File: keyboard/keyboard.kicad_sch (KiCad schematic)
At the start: 29 parts, among them SW10 KH-6X6X6H-STM, SW11 KH-6X6X6H-STM, SW12 KH-6X6X6H-STM, SW13 KH-6X6X6H-STM, SW14 KH-6X6X6H-STM, SW3 KH-6X6X6H-STM, SW4 KH-6X6X6H-STM, SW5 KH-6X6X6H-STM, SW6 KH-6X6X6H-STM, SW7 KH-6X6X6H-STM, SW8 KH-6X6X6H-STM, SW9 KH-6X6X6H-STM, U12 TM1638

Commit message: feat: 新增点阵屏键盘小板
新增点阵屏小板的工程，并删除主项目的 sch
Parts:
- removed C19: 100pF, Capacitor_SMD:C_0603_1608Metric, symbol Device:C
- removed R11: 10k, PCM_SparkFun-Resistor:R_0603_1608Metric, symbol PCM_SparkFun-Resistor:R
- added FPC1: HC-FPC-05-10-5RLTAG, lcsc_footprints:C5213728_FPC-SMD_5P-P0_50_HCTL_HC-FPC-05-10-5RLTAG, symbol lcsc_imported:HC-FPC-05-10-5RLTAG
- D3, D4, D5, D6, D7, D8: footprint PCM_Diode_SMD_AKL:D_SOD-123 -> Diode_SMD:D_SOD-123
- R12, R13: footprint PCM_SparkFun-Resistor:R_0603_1608Metric -> Resistor_SMD:R_0603_1608Metric
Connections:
- net 5V_IN: now also FPC1.1
- net GND_IN: now also FPC1.2
- net CLK: no longer names the net of C20.1, R12.1, U12.27 (CLK)
- net CLK: now also FPC1.4
- net DIO: no longer names the net of C21.1, R13.1, U12.26 (DIO)
- net DIO: now also FPC1.5
- net STB: no longer names the net of U12.28 (STB)
- net STB: now also FPC1.3
- no-connect marks 19 -> 21
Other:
- moved on the sheet: C22, C23

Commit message: update: 添加按键小板电源指示灯并优化布线
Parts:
- added D1: LED, LED_SMD:LED_0603_1608Metric, symbol Device:LED
- added R14: 4.7k, Resistor_SMD:R_0603_1608Metric, symbol PCM_SparkFun-Resistor:R
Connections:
- net 5V_IN renamed +5V
- net +5V: now also D1.2 (A)
- net GND_IN renamed GND
- net GND: now also R14.1
- new net: D1.1 (K), R14.2

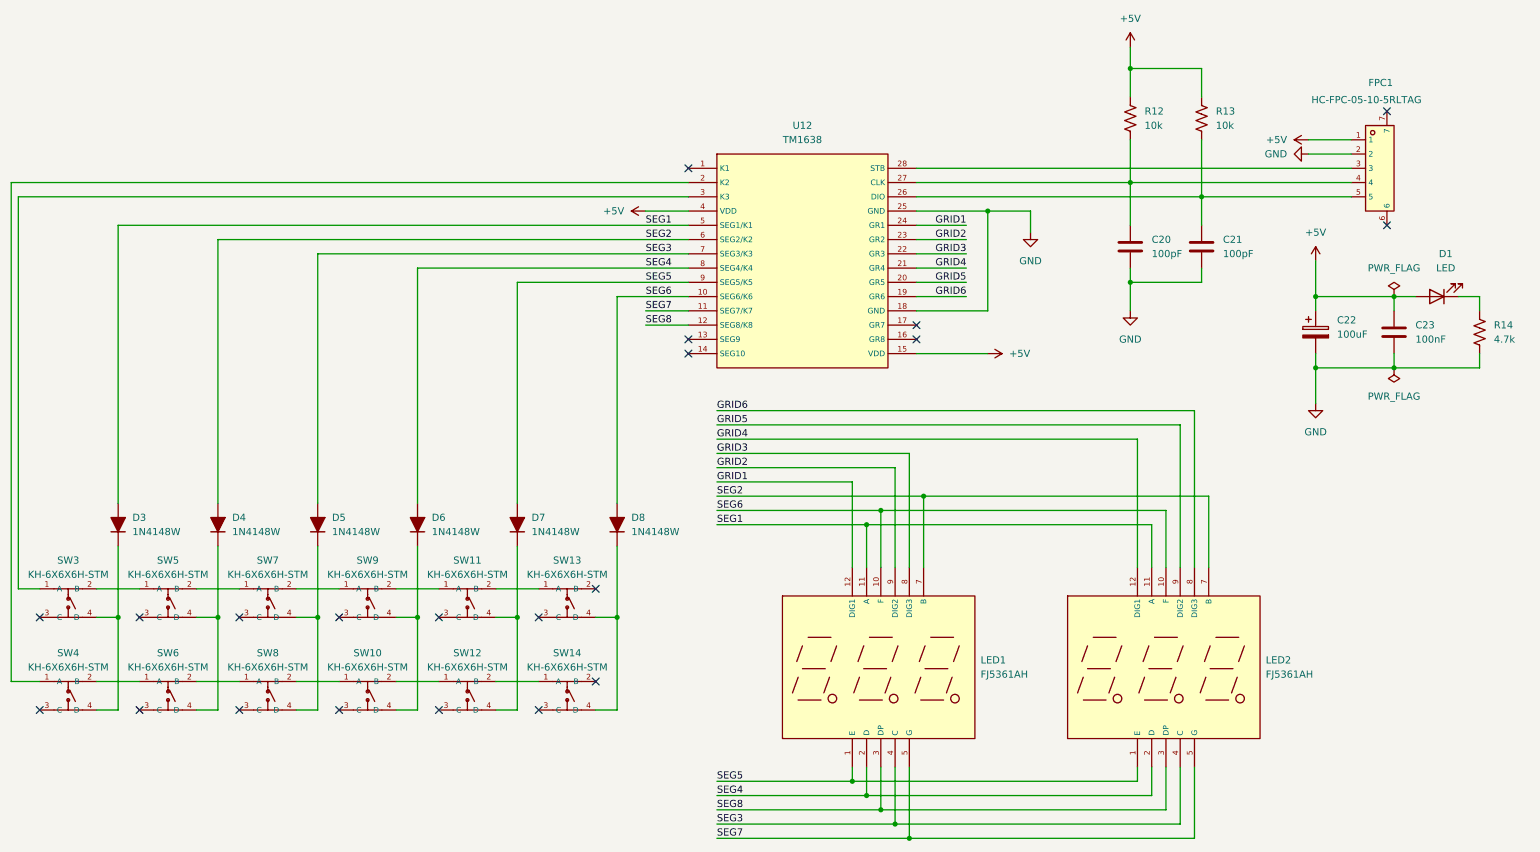
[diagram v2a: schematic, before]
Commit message: update: 更新按钮小板设计，导出gerber文件
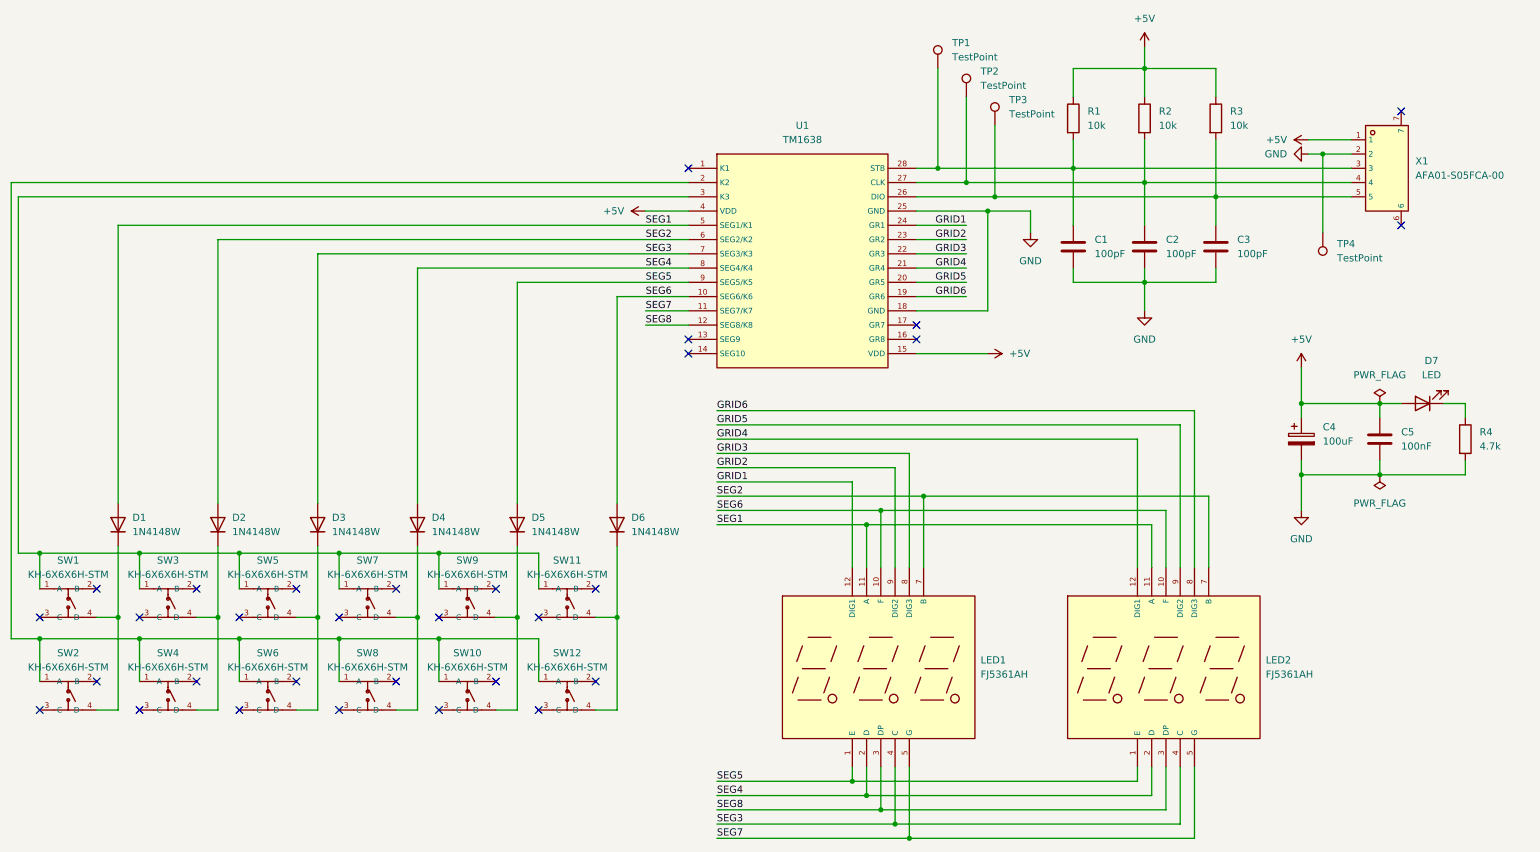
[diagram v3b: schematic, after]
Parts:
- removed D3, D4, D5, D6, D7, D8: 1N4148W, Diode_SMD:D_SOD-123, symbol PCM_Diode_AKL:1N4148W
- removed FPC1: HC-FPC-05-10-5RLTAG, lcsc_footprints:C5213728_FPC-SMD_5P-P0_50_HCTL_HC-FPC-05-10-5RLTAG, symbol lcsc_imported:HC-FPC-05-10-5RLTAG
- removed R12, R13: 10k, Resistor_SMD:R_0603_1608Metric, symbol PCM_SparkFun-Resistor:R
- removed R14: 4.7k, Resistor_SMD:R_0603_1608Metric, symbol PCM_SparkFun-Resistor:R
- added C1: 100pF, Capacitor_SMD:C_0603_1608Metric, symbol Device:C
- added D1, D2, D3, D4, D5, D6: 1N4148W, Diode_SMD:D_SOD-123, symbol Diode:1N4148W
- added R1, R2, R3: 10k, Resistor_SMD:R_0603_1608Metric, symbol Device:R
- added R4: 4.7k, Resistor_SMD:R_0603_1608Metric, symbol Device:R
- added TP1, TP2, TP3, TP4: TestPoint, TestPoint:TestPoint_Pad_D2.0mm, symbol Connector:TestPoint
- added X1: AFA01-S05FCA-00, lcsc_footprints:C262753_FPC-SMD_AFA01-S05FCA-00, symbol lcsc_imported:AFA01-S05FCA-00
- renumbered C20 to C2, C21 to C3, C22 to C4, C23 to C5, D1 to D7, SW3 to SW1, SW12 to SW10, SW13 to SW11, SW14 to SW12, SW4 to SW2, SW5 to SW3, SW6 to SW4, SW7 to SW5, SW8 to SW6, SW9 to SW7, SW10 to SW8, SW11 to SW9, U12 to U1
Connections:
- net +5V: now also R1.1, R2.1, R3.1, X1.1
- net GND: now also C1.2, R4.2, TP4.1, X1.2
- net SEG1: now also D1.2 (A)
- net SEG2: now also D2.2 (A)
- net SEG3: now also D3.2 (A)
- net SEG4: now also D4.2 (A)
- net SEG5: now also D5.2 (A)
- net SEG6: now also D6.2 (A)
- net at SW4.1 (A): now also SW10.1 (A), SW12.1 (A), SW2.1 (A), SW6.1 (A), SW8.1 (A), U1.2 (K2); no longer SW2.2 (B)
- net at SW4.2 (B): no longer SW6.1 (A)
- net at SW3.4 (D), SW4.4 (D): now also D2.1 (K)
- net at SW1.4 (D), SW2.4 (D): now also D1.1 (K)
- net at SW11.4 (D), SW12.4 (D): now also D6.1 (K)
- net at SW5.4 (D), SW6.4 (D): now also D3.1 (K)
- net at SW1.1 (A), U1.3 (K3): now also SW11.1 (A), SW3.1 (A), SW5.1 (A), SW7.1 (A), SW9.1 (A)
- net at SW1.2 (B): no longer SW3.1 (A)
- net at C3.1, U1.26 (DIO): now also R3.2, TP3.1, X1.5
- net at SW8.2 (B): no longer SW10.1 (A)
- net at SW10.2 (B): no longer SW12.1 (A)
- net at SW10.4 (D), SW9.4 (D): now also D5.1 (K)
- net at SW7.2 (B): no longer SW9.1 (A)
- net at SW9.2 (B): no longer SW11.1 (A)
- net at C2.1, U1.27 (CLK): now also R2.2, TP2.1, X1.4
- net at SW3.2 (B): no longer SW5.1 (A)
- net at SW5.2 (B): no longer SW7.1 (A)
- net at U1.28 (STB): now also C1.1, R1.2, TP1.1, X1.3
- net at D7.1 (K): now also R4.1
- net at SW7.4 (D), SW8.4 (D): now also D4.1 (K)
- net at SW6.2 (B): no longer SW8.1 (A)
- no-connect marks 21 -> 31
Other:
- moved on the sheet: C2, C3, C4, C5, D7
